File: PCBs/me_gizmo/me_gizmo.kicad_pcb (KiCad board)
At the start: 2 copper layers, 28.5 x 63.8 mm, 36 parts, among them J2 Conn_01x24_Pin, J3 Conn_01x09_Pin, J4 Conn_01x07_Pin, U1 ADG714, U2 ADG714, U3 ADG714, U4 ADG714, U5 XS3A4053, U6 XS3A4053

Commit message: First draft on the schematic for the final device
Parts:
- added C1: 1µF, Capacitor_SMD:C_0402_1005Metric, F.Cu at (63.0, 69.3)
- added C10: 0.1µF, Capacitor_SMD:C_0402_1005Metric, F.Cu at (65.9, 73.3)
- added C11: 4.7µF, Eclectronics:C_0402_1005Metric, F.Cu at (65.9, 75.2)
- added C12: 4.7µF, Capacitor_SMD:C_0402_1005Metric, F.Cu at (65.9, 77.2)
- added C13: 4.7µF, Eclectronics:C_0402_1005Metric, F.Cu at (68.7, 69.3)
- added C14: 0.1µF, Capacitor_SMD:C_0402_1005Metric, F.Cu at (68.7, 71.3)
- added C15: 4.7µF, Capacitor_SMD:C_0402_1005Metric, F.Cu at (68.7, 73.3)
- added C16: 0.1µF, Capacitor_SMD:C_0402_1005Metric, F.Cu at (68.7, 75.2)
- added C17: 1µF, Capacitor_SMD:C_0603_1608Metric, F.Cu at (54.8, 84.6)
- added C18: 1µF, Capacitor_SMD:C_0603_1608Metric, F.Cu at (54.8, 87.1)
- added C19: 0.1µF, Capacitor_SMD:C_0603_1608Metric, F.Cu at (54.8, 89.6)
- added C2: 10µF, Capacitor_SMD:C_0603_1608Metric, F.Cu at (54.8, 79.5)
- added C22: 0.1µF, Capacitor_SMD:C_0603_1608Metric, F.Cu at (43.6, 99.5)
- added C23: 1µF, Capacitor_SMD:C_0603_1608Metric, F.Cu at (43.6, 102.0)
- added C24: 1µF, Capacitor_SMD:C_0603_1608Metric, F.Cu at (43.6, 104.5)
- added C25: 1µF, Capacitor_SMD:C_0603_1608Metric, F.Cu at (43.6, 107.0)
- added C26: 0.1µF, Capacitor_SMD:C_0603_1608Metric, F.Cu at (43.6, 109.5)
- added C27: 0.1µF, Capacitor_SMD:C_0603_1608Metric, F.Cu at (43.6, 112.0)
- added C28: 0.1µF, Capacitor_SMD:C_0603_1608Metric, F.Cu at (47.6, 99.5)
- added C29: 0.1µF, Capacitor_SMD:C_0603_1608Metric, F.Cu at (47.6, 102.0)
- added C3: 10µF, Capacitor_SMD:C_0603_1608Metric, F.Cu at (54.8, 82.1)
- added C30: 0.1µF, Capacitor_SMD:C_0603_1608Metric, F.Cu at (47.6, 104.5)
- added C31: 0.1µF, Capacitor_SMD:C_0603_1608Metric, F.Cu at (47.6, 107.0)
- added C32: 0.1µF, Capacitor_SMD:C_0603_1608Metric, F.Cu at (47.6, 109.5)
- added C33: 0.1µF, Capacitor_SMD:C_0603_1608Metric, F.Cu at (47.6, 112.0)
- added C34: 0.1µF, Capacitor_SMD:C_0603_1608Metric, F.Cu at (51.6, 99.5)
- added C35: 0.1µF, Capacitor_SMD:C_0603_1608Metric, F.Cu at (51.6, 102.0)
- added C36: 0.1µF, Capacitor_SMD:C_0603_1608Metric, F.Cu at (51.6, 104.5)
- added C37: 0.1µF, Capacitor_SMD:C_0603_1608Metric, F.Cu at (51.6, 107.0)
- added C4: 0.1µF, Capacitor_SMD:C_0402_1005Metric, F.Cu at (63.0, 71.3)
- added C41: 0.1u, Capacitor_SMD:C_0603_1608Metric, F.Cu at (95.3, 99.5)
- added C42: 0.1u, Capacitor_SMD:C_0603_1608Metric, F.Cu at (95.3, 102.0)
- added C43: 0.1u, Capacitor_SMD:C_0603_1608Metric, F.Cu at (95.3, 104.5)
- added C44: 0.1u, Capacitor_SMD:C_0603_1608Metric, F.Cu at (95.3, 107.0)
- added C5: 0.1µF, Capacitor_SMD:C_0402_1005Metric, F.Cu at (63.0, 73.3)
- added C6: 0.1µF, Capacitor_SMD:C_0402_1005Metric, F.Cu at (63.0, 75.2)
- added C7: 0.1µF, Capacitor_SMD:C_0402_1005Metric, F.Cu at (63.0, 77.2)
- added C8: 0.1µF, Capacitor_SMD:C_0402_1005Metric, F.Cu at (65.9, 69.3)
- added C9: 0.1µF, Capacitor_SMD:C_0402_1005Metric, F.Cu at (65.9, 71.3)
- added D1: LED, LED_SMD:LED_0805_2012Metric, F.Cu at (69.5, 79.8)
- added D2: IN-S85TATRGB, Eclectronics:IN-S85TATRGB, F.Cu at (69.9, 85.7)
- added D3: PWR, LED_SMD:LED_0805_2012Metric, F.Cu at (69.5, 82.8)
- added J1: PushButton_Terminal_01x06, Eclectronics:CONN5_233-505_WAG, F.Cu at (79.7, 81.0)
- added J5: DEBUG, Connector_PinHeader_2.54mm:PinHeader_1x03_P2.54mm_Vertical, F.Cu at (65.0, 80.6)
- added J6: USB4105-GF-A, Eclectronics:USB4105-GF-A, F.Cu at (47.2, 74.4)
- added L1: 3.3µH, Eclectronics:AOTA-B201610S3R3-101-T, F.Cu at (44.3, 93.9)
- added Q3: MBT3904DW1, Package_TO_SOT_SMD:SOT-363_SC-70-6, F.Cu at (48.6, 90.0)
- added R10: 348, Resistor_SMD:R_0603_1608Metric, F.Cu at (43.6, 124.6)
- added R11: 118, Resistor_SMD:R_0603_1608Metric, F.Cu at (43.6, 127.1)
- added R12: 118, Resistor_SMD:R_0603_1608Metric, F.Cu at (43.6, 129.6)
- added R13: 348, Resistor_SMD:R_0603_1608Metric, F.Cu at (43.6, 132.1)
- added R14: 348, Resistor_SMD:R_0603_1608Metric, F.Cu at (43.6, 134.6)
- added R15: 118, Resistor_SMD:R_0603_1608Metric, F.Cu at (43.6, 137.2)
- added R16: 348, Resistor_SMD:R_0603_1608Metric, F.Cu at (70.4, 99.5)
- added R17: 118, Resistor_SMD:R_0603_1608Metric, F.Cu at (70.4, 102.0)
- added R18: 118, Resistor_SMD:R_0603_1608Metric, F.Cu at (70.4, 104.5)
- added R4: 348, Resistor_SMD:R_0603_1608Metric, F.Cu at (94.9, 78.9)
- added R43: 100Ω, Resistor_SMD:R_0603_1608Metric, F.Cu at (55.6, 112.0)
- added R44: 5.1K, Resistor_SMD:R_0402_1005Metric, F.Cu at (57.2, 75.3)
- added R45: 1K, Resistor_SMD:R_0402_1005Metric, F.Cu at (57.2, 77.3)
- added R46: 1K, Resistor_SMD:R_0402_1005Metric, F.Cu at (60.1, 69.3)
- added R47: 1K, Resistor_SMD:R_0402_1005Metric, F.Cu at (60.1, 71.3)
- added R48: 10k, Resistor_SMD:R_0402_1005Metric, F.Cu at (60.1, 73.3)
- added R5: 118, Resistor_SMD:R_0603_1608Metric, F.Cu at (94.9, 81.5)
- added R6: 118, Resistor_SMD:R_0603_1608Metric, F.Cu at (94.9, 84.0)
- added R7: 348, Resistor_SMD:R_0603_1608Metric, F.Cu at (94.9, 86.5)
- added R8: 348, Resistor_SMD:R_0603_1608Metric, F.Cu at (94.9, 89.0)
- added R9: 118, Resistor_SMD:R_0603_1608Metric, F.Cu at (94.9, 91.5)
- added S1: RST, Button_Switch_SMD:SW_SPST_B3U-1000P, F.Cu at (59.8, 80.5)
- added S2: BOOT, Button_Switch_SMD:SW_SPST_B3U-1000P, F.Cu at (59.8, 84.8)
- added U10: RP2350A, Eclectronics:RP2350A_QFN-60_EP_7.75x7.75_Pitch0.4mm, F.Cu at (116.6, 94.4)
- added U11: MCP4922, Package_SO:TSSOP-14_4.4x5mm_P0.65mm, F.Cu at (62.0, 101.5)
- added U12: MCP4922, Package_SO:TSSOP-14_4.4x5mm_P0.65mm, F.Cu at (62.0, 108.1)
- added U13: MCP1702T-3302E_CB, Package_TO_SOT_SMD:SOT-23, F.Cu at (44.0, 90.4)
- added U7: TLV9152VSSOP, Package_SO:VSSOP-8_3x3mm_P0.65mm, F.Cu at (66.4, 90.3)
- added U9: MCP3564R, Package_SO:TSSOP-20_4.4x6.5mm_P0.65mm, F.Cu at (46.3, 117.3)
- added X1: IQXO-791, Eclectronics:IQXO-791, F.Cu at (49.0, 93.5)
- added X4: SG-8018CG_19.6608M-TJHSA3, Crystal:Crystal_SMD_2520-4Pin_2.5x2.0mm, F.Cu at (53.0, 115.3)
- J2: value Conn_01x24_Pin -> PushButton_Terminal_01x06; footprint Connector_PinHeader_2.54mm:PinHeader_1x24_P2.54mm_Vertical -> Eclectronics:CONN5_233-505_WAG
- J3: value Conn_01x09_Pin -> PushButton_Terminal_01x06; footprint Connector_PinHeader_2.54mm:PinHeader_1x09_P2.54mm_Vertical -> Eclectronics:CONN5_233-505_WAG
- J4: value Conn_01x07_Pin -> PushButton_Terminal_01x06; footprint Connector_PinHeader_2.54mm:PinHeader_1x07_P2.54mm_Vertical -> Eclectronics:CONN5_233-505_WAG
- R1, R2, R3: value R -> 10k; footprint Resistor_SMD:R_0603_1608Metric -> Resistor_SMD:R_0402_1005Metric_Pad0.72x0.64mm_HandSolder
- R19, R20, R22: value 120 -> 348
- R21: value 120 -> 118
- R23, R24, R27: value 350 -> 118
- R25, R26: value 350 -> 348
- R28, R29, R30, R31: value 350 -> 5.1K; footprint Resistor_SMD:R_0603_1608Metric -> Resistor_SMD:R_0402_1005Metric
- R32, R33: value 350 -> 27Ω; footprint Resistor_SMD:R_0603_1608Metric -> Resistor_SMD:R_0402_1005Metric
- R34: value 350 -> 33Ω; footprint Resistor_SMD:R_0603_1608Metric -> Resistor_SMD:R_0402_1005Metric
- R35: value 120 -> 1K; footprint Resistor_SMD:R_0603_1608Metric -> Resistor_SMD:R_0402_1005Metric
- R36, R37, R38, R39, R40, R41, R42: value 120 -> 100Ω
- U5: value XS3A4053 -> REF35250QDBVR; footprint Multiplexer:TSSOP-16 -> Package_TO_SOT_SMD:SOT-23-6
- U6: value XS3A4053 -> TMP126-Q1; footprint Multiplexer:TSSOP-16 -> Package_TO_SOT_SMD:SOT-23-6
- moved J2 86.6 mm to (51.3, 126.7)
- moved R28 84.4 mm to (54.3, 69.3), turned to 0 degrees
- moved R35 82.9 mm to (57.2, 73.3), turned to 0 degrees
- moved U2 80.7 mm to (87.9, 73.0), turned to 0 degrees
- moved R29 79.9 mm to (54.3, 71.3)
- moved U5 78.2 mm to (59.4, 89.4)
- moved R42 78.1 mm to (55.6, 109.5), turned to 0 degrees
- moved R40 77.6 mm to (55.6, 104.5), turned to 0 degrees
- moved R30 77.2 mm to (54.3, 73.3), turned to 0 degrees
- moved R37 76.3 mm to (51.6, 112.0)
- moved R32 76.2 mm to (54.3, 77.3), turned to 0 degrees
- moved R36 75.9 mm to (51.6, 109.5), turned to 0 degrees
- moved R41 75.4 mm to (55.6, 107.0), turned to 0 degrees
- moved R31 74.8 mm to (54.3, 75.3), turned to 0 degrees
- moved U1 73.9 mm to (78.7, 73.0), turned to 0 degrees
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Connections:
- J2 pad 1: /Wheatstone Bridge 1/HB_OUT1+ -> VREF_BUF
- J2 pad 10: /Wheatstone Bridge 1/2ADC_IN2+ -> (no net)
- J2 pad 2: /Wheatstone Bridge 1/2ADC_IN1- -> /ADC/DAC/CH2/HB2+
- J2 pad 3: /Wheatstone Bridge 1/HB_OUT1- -> /ADC/DAC/CH2/ADC2+
- J2 pad 4: /Wheatstone Bridge 1/2ADC_IN1+ -> /ADC/DAC/CH2/HB2-
- J2 pad 5: /Wheatstone Bridge 1/2.5V -> /ADC/DAC/CH2/ADC2-
- J2 pad 7: /Wheatstone Bridge 1/HB_OUT2+ -> (no net)
- J2 pad 8: /Wheatstone Bridge 1/2ADC_IN2- -> (no net)
- J2 pad 9: /Wheatstone Bridge 1/HB_OUT2- -> (no net)
- J3 pad 1: /Wheatstone Bridge 1/2ADC_IN4- -> VREF_BUF
- J3 pad 2: /Wheatstone Bridge 1/2ADC_IN4+ -> /ADC/DAC/CH3/HB3+
- J3 pad 3: /Wheatstone Bridge 1/2ADC_IN3- -> /ADC/DAC/CH3/ADC3+
- J3 pad 4: /Wheatstone Bridge 1/2ADC_IN3+ -> /ADC/DAC/CH3/HB3-
- J3 pad 5: /Wheatstone Bridge 1/2ADC_IN2- -> /ADC/DAC/CH3/ADC3-
- J3 pad 6: /Wheatstone Bridge 1/2ADC_IN2+ -> GND
- J3 pad 7: /Wheatstone Bridge 1/2ADC_IN1- -> (no net)
- J3 pad 8: /Wheatstone Bridge 1/2ADC_IN1+ -> (no net)
- J3 pad 9: /Wheatstone Bridge 1/2.5V -> (no net)
- J4 pad 1: /Wheatstone Bridge 1/CIPO -> VREF_BUF
- J4 pad 2: /Wheatstone Bridge 1/VDD -> /ADC/DAC/CH4/HB4+
- J4 pad 3: /Wheatstone Bridge 1/SCLK -> /ADC/DAC/CH4/ADC4+
- J4 pad 4: /Wheatstone Bridge 1/RESET -> /ADC/DAC/CH4/HB4-
- J4 pad 5: /Wheatstone Bridge 1/CS -> /ADC/DAC/CH4/ADC4-
- J4 pad 6: /Wheatstone Bridge 1/Rselect1 -> GND
- J4 pad 7: /Wheatstone Bridge 1/Rselect2 -> (no net)
- R1 pad 1: Net-(U2-DOUT) -> +5V
- R1 pad 2: /Wheatstone Bridge 1/VDD -> Net-(U1I-DOUT)
- R19 pad 1: /Wheatstone Bridge 1/RI1 -> GND
- R19 pad 2: /Wheatstone Bridge 1/HB_OUT3- -> Net-(U4F-D)
- R2 pad 1: /Wheatstone Bridge 1/VDD -> +5V
- R2 pad 2: Net-(U3-DOUT) -> Net-(U2I-DOUT)
- R20 pad 1: /Wheatstone Bridge 1/RJ1 -> GND
- R20 pad 2: GND -> Net-(U4E-D)
- R21 pad 1: /Wheatstone Bridge 1/RK1 -> Net-(U4D-D)
- R22 pad 1: /Wheatstone Bridge 1/RL1 -> Net-(U1C-S)
- R22 pad 2: /Wheatstone Bridge 1/HB_OUT4- -> /ADC/DAC/CH4/HB4-
- R23 pad 1: /Wheatstone Bridge 1/RI2 -> Net-(U1D-S)
- R23 pad 2: /Wheatstone Bridge 1/HB_OUT3- -> /ADC/DAC/CH4/HB4-
- R24 pad 1: /Wheatstone Bridge 1/RJ2 -> Net-(U4A-D)
- R25 pad 1: /Wheatstone Bridge 1/RK2 -> GND
- R25 pad 2: GND -> Net-(U4H-D)
- R26 pad 1: /Wheatstone Bridge 1/RL2 -> GND
- R26 pad 2: /Wheatstone Bridge 1/HB_OUT4- -> Net-(U4G-D)
- R27 pad 1: /Wheatstone Bridge 1/RH2 -> Net-(U4B-D)
- R28 pad 1: /Wheatstone Bridge 1/RG2 -> +3V3
- R28 pad 2: GND -> /RUN
- R29 pad 1: /Wheatstone Bridge 1/RF2 -> +3V3
- R29 pad 2: /Wheatstone Bridge 1/HB_OUT2- -> /BOOT
- R3 pad 1: Net-(U1-DOUT) -> +5V
- R3 pad 2: /Wheatstone Bridge 1/VDD -> Net-(U3I-DOUT)
- R30 pad 1: /Wheatstone Bridge 1/RE2 -> Net-(J6-CC2)
- R31 pad 1: /Wheatstone Bridge 1/RD2 -> Net-(J6-CC1)
- R32 pad 1: /Wheatstone Bridge 1/RC2 -> Net-(J6-D--PadA7)
- R32 pad 2: /Wheatstone Bridge 1/HB_OUT1- -> Net-(U10-USB_D-)
- R33 pad 1: /Wheatstone Bridge 1/RB2 -> Net-(J6-D+-PadA6)
- R33 pad 2: GND -> Net-(U10-USB_D+)
- R34 pad 1: /Wheatstone Bridge 1/RA2 -> Net-(U10-VREG_AVDD)
- R34 pad 2: GND -> +3V3
- R35 pad 1: /Wheatstone Bridge 1/RH1 -> /GPIO22
- R35 pad 2: GND -> Net-(D2-Pad1)
- R36 pad 1: /Wheatstone Bridge 1/RG1 -> Net-(U9-CH7)
- R36 pad 2: GND -> /ADC/DAC/CH4/ADC4-
- R37 pad 1: /Wheatstone Bridge 1/RF1 -> Net-(U9-CH6)
- R37 pad 2: /Wheatstone Bridge 1/HB_OUT2- -> /ADC/DAC/CH4/ADC4+
- R38 pad 1: /Wheatstone Bridge 1/RE1 -> Net-(U9-CH5)
- R38 pad 2: GND -> /ADC/DAC/CH3/ADC3-
- R39 pad 1: /Wheatstone Bridge 1/RD1 -> Net-(U9-CH4)
- R39 pad 2: GND -> /ADC/DAC/CH3/ADC3+
- R40 pad 1: /Wheatstone Bridge 1/RC1 -> Net-(U9-CH3)
- R40 pad 2: /Wheatstone Bridge 1/HB_OUT1- -> /ADC/DAC/CH2/ADC2-
- R41 pad 1: /Wheatstone Bridge 1/RB1 -> Net-(U9-CH2)
- R41 pad 2: GND -> /ADC/DAC/CH2/ADC2+
- R42 pad 1: /Wheatstone Bridge 1/RA1 -> Net-(U9-CH1)
- R42 pad 2: GND -> /ADC/DAC/CH1/ADC1-
- U1 pad 1: /Wheatstone Bridge 1/SCLK -> SCLK
- U1 pad 10: /Wheatstone Bridge 1/branch5 -> VREF_BUF
- U1 pad 11: /Wheatstone Bridge 1/2.5V -> Net-(U1D-S)
- U1 pad 12: /Wheatstone Bridge 1/branch4 -> VREF_BUF
- U1 pad 13: /Wheatstone Bridge 1/branch3 -> Net-(U1E-D)
- U1 pad 14: /Wheatstone Bridge 1/HB_OUT1- -> VREF_BUF
- U1 pad 15: /Wheatstone Bridge 1/branch6 -> Net-(U1F-D)
- U1 pad 16: /Wheatstone Bridge 1/HB_OUT2- -> VREF_BUF
- U1 pad 17: /Wheatstone Bridge 1/branch7 -> Net-(U1G-D)
- U1 pad 18: /Wheatstone Bridge 1/HB_OUT3+ -> VREF_BUF
- U1 pad 19: /Wheatstone Bridge 1/branch8 -> Net-(U1H-D)
- U1 pad 2: /Wheatstone Bridge 1/VDD -> +5V
- U1 pad 20: /Wheatstone Bridge 1/HB_OUT3- -> VREF_BUF
- U1 pad 22: Net-(U1-DOUT) -> Net-(U1I-DOUT)
- U1 pad 23: /Wheatstone Bridge 1/RESET -> /RESET
- U1 pad 24: /Wheatstone Bridge 1/CS -> /SYNC
- U1 pad 3: /Wheatstone Bridge 1/CIPO -> COPI
- U1 pad 5: /Wheatstone Bridge 1/HB_OUT1+ -> Net-(U1A-S)
- U1 pad 6: /Wheatstone Bridge 1/branch2 -> VREF_BUF
- U1 pad 7: /Wheatstone Bridge 1/2.5V -> Net-(U1B-S)
- U1 pad 8: /Wheatstone Bridge 1/branch1 -> VREF_BUF
- U1 pad 9: /Wheatstone Bridge 1/HB_OUT2+ -> Net-(U1C-S)
- U2 pad 1: /Wheatstone Bridge 1/SCLK -> SCLK
- U2 pad 10: /Wheatstone Bridge 1/branch10 -> Net-(U2C-D)
- U2 pad 11: /Wheatstone Bridge 1/2.5V -> Net-(U2D-S)
- U2 pad 12: /Wheatstone Bridge 1/branch9 -> /ADC/DAC/CH1/HB1+
- U2 pad 13: /Wheatstone Bridge 1/RI1 -> /ADC/DAC/CH1/HB1+
- U2 pad 14: /Wheatstone Bridge 1/branch9 -> Net-(U2E-S)
- U2 pad 15: /Wheatstone Bridge 1/RJ1 -> /ADC/DAC/CH1/HB1-
- U2 pad 16: /Wheatstone Bridge 1/branch10 -> Net-(U2F-S)
- U2 pad 17: /Wheatstone Bridge 1/RK1 -> Net-(U2G-D)
- U2 pad 18: /Wheatstone Bridge 1/branch11 -> /ADC/DAC/CH2/HB2+
- U2 pad 19: /Wheatstone Bridge 1/RL1 -> Net-(U2H-D)
- U2 pad 2: /Wheatstone Bridge 1/VDD -> +5V
- U2 pad 20: /Wheatstone Bridge 1/branch12 -> /ADC/DAC/CH2/HB2-
- U2 pad 22: Net-(U2-DOUT) -> Net-(U2I-DOUT)
- U2 pad 23: /Wheatstone Bridge 1/RESET -> /RESET
- U2 pad 24: /Wheatstone Bridge 1/CS -> /SYNC
- U2 pad 3: Net-(U1-DOUT) -> Net-(U1I-DOUT)
- U2 pad 5: /Wheatstone Bridge 1/2.5V -> /ADC/DAC/CH2/HB2-
- U2 pad 6: /Wheatstone Bridge 1/branch12 -> Net-(U2A-D)
- U2 pad 7: /Wheatstone Bridge 1/HB_OUT4- -> /ADC/DAC/CH2/HB2+
- U2 pad 8: /Wheatstone Bridge 1/branch11 -> Net-(U2B-D)
- U2 pad 9: /Wheatstone Bridge 1/HB_OUT4+ -> /ADC/DAC/CH1/HB1-
- U3 pad 1: /Wheatstone Bridge 1/SCLK -> SCLK
- U3 pad 10: /Wheatstone Bridge 1/2ADC_IN4+ -> /ADC/DAC/CH2/ADC2+
- U3 pad 11: /Wheatstone Bridge 1/HB_OUT4- -> /ADC/DAC/CH2/HB2-
- U3 pad 12: /Wheatstone Bridge 1/2ADC_IN4- -> /ADC/DAC/CH2/ADC2-
- U3 pad 13: /Wheatstone Bridge 1/2ADC_IN2- -> /ADC/DAC/CH3/ADC3+
- U3 pad 14: /Wheatstone Bridge 1/HB_OUT2- -> /ADC/DAC/CH3/HB3+
- U3 pad 15: /Wheatstone Bridge 1/2ADC_IN2+ -> /ADC/DAC/CH3/ADC3-
- U3 pad 16: /Wheatstone Bridge 1/HB_OUT2+ -> /ADC/DAC/CH3/HB3-
- U3 pad 17: /Wheatstone Bridge 1/2ADC_IN1- -> /ADC/DAC/CH4/ADC4+
- U3 pad 18: /Wheatstone Bridge 1/HB_OUT1- -> /ADC/DAC/CH4/HB4+
- U3 pad 19: /Wheatstone Bridge 1/2ADC_IN1+ -> /ADC/DAC/CH4/ADC4-
- U3 pad 2: /Wheatstone Bridge 1/VDD -> +5V
- U3 pad 20: /Wheatstone Bridge 1/HB_OUT1+ -> /ADC/DAC/CH4/HB4-
- U3 pad 22: Net-(U3-DOUT) -> Net-(U3I-DOUT)
- U3 pad 23: /Wheatstone Bridge 1/RESET -> /RESET
- U3 pad 24: /Wheatstone Bridge 1/CS -> /SYNC
- U3 pad 3: Net-(U2-DOUT) -> Net-(U2I-DOUT)
- U3 pad 5: /Wheatstone Bridge 1/HB_OUT3+ -> /ADC/DAC/CH1/HB1+
- U3 pad 6: /Wheatstone Bridge 1/2ADC_IN3+ -> /ADC/DAC/CH1/ADC1+
- U3 pad 7: /Wheatstone Bridge 1/HB_OUT3- -> /ADC/DAC/CH1/HB1-
- U3 pad 8: /Wheatstone Bridge 1/2ADC_IN3- -> /ADC/DAC/CH1/ADC1-
- U3 pad 9: /Wheatstone Bridge 1/HB_OUT4+ -> /ADC/DAC/CH2/HB2+
- U4 pad 1: /Wheatstone Bridge 1/SCLK -> SCLK
- U4 pad 10: /Wheatstone Bridge 1/RG2 -> Net-(U4C-D)
- U4 pad 11: /Wheatstone Bridge 1/branch8 -> /ADC/DAC/CH3/HB3+
- U4 pad 12: /Wheatstone Bridge 1/RH2 -> Net-(U4D-D)
- U4 pad 13: /Wheatstone Bridge 1/RI2 -> Net-(U4E-D)
- U4 pad 14: /Wheatstone Bridge 1/branch9 -> /ADC/DAC/CH3/HB3+
- U4 pad 15: /Wheatstone Bridge 1/RJ2 -> Net-(U4F-D)
- U4 pad 16: /Wheatstone Bridge 1/branch10 -> /ADC/DAC/CH3/HB3-
- U4 pad 17: /Wheatstone Bridge 1/RK2 -> Net-(U4G-D)
- U4 pad 18: /Wheatstone Bridge 1/branch11 -> /ADC/DAC/CH4/HB4+
- U4 pad 19: /Wheatstone Bridge 1/RL2 -> Net-(U4H-D)
- U4 pad 2: /Wheatstone Bridge 1/VDD -> +5V
- U4 pad 20: /Wheatstone Bridge 1/branch12 -> /ADC/DAC/CH4/HB4-
- U4 pad 23: /Wheatstone Bridge 1/RESET -> /RESET
- U4 pad 24: /Wheatstone Bridge 1/CS -> /SYNC
- U4 pad 3: Net-(U3-DOUT) -> Net-(U3I-DOUT)
- U4 pad 5: /Wheatstone Bridge 1/branch8 -> /ADC/DAC/CH4/HB4-
- U4 pad 6: /Wheatstone Bridge 1/RH1 -> Net-(U4A-D)
- U4 pad 7: /Wheatstone Bridge 1/branch7 -> /ADC/DAC/CH4/HB4+
- U4 pad 8: /Wheatstone Bridge 1/RG1 -> Net-(U4B-D)
- U4 pad 9: /Wheatstone Bridge 1/branch7 -> /ADC/DAC/CH3/HB3-
- U5 pad 1: /Wheatstone Bridge 1/RD1 -> GND
- U5 pad 2: /Wheatstone Bridge 1/RD2 -> GND
- U5 pad 3: /Wheatstone Bridge 1/RE1 -> +3V3
- U5 pad 4: /Wheatstone Bridge 1/branch6 -> +3V3
- U5 pad 5: /Wheatstone Bridge 1/RE2 -> unconnected-(U5-NR-Pad5)
- U5 pad 6: GND -> /VREF
- U6 pad 1: /Wheatstone Bridge 1/RA1 -> /TEMP_CS
- U6 pad 2: /Wheatstone Bridge 1/RA2 -> GND
- U6 pad 3: /Wheatstone Bridge 1/RB1 -> /CIPO
- U6 pad 4: /Wheatstone Bridge 1/branch3 -> SCLK
- U6 pad 5: /Wheatstone Bridge 1/RB2 -> +3V3
- U6 pad 6: GND -> +3V3
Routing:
- net /Wheatstone Bridge 1/2.5V: track 147.9 -> 0.00 mm, vias 7 -> 0
- net /Wheatstone Bridge 1/CS: track 66.0 -> 0.00 mm, vias 4 -> 0
- net /Wheatstone Bridge 1/HB_OUT1+: track 64.5 -> 0.00 mm, vias 4 -> 0
- net /Wheatstone Bridge 1/RESET: track 60.6 -> 0.00 mm, vias 4 -> 0
- net /Wheatstone Bridge 1/HB_OUT3-: track 59.7 -> 0.00 mm, vias 3 -> 0
- net /Wheatstone Bridge 1/HB_OUT4-: track 58.4 -> 0.00 mm, vias 5 -> 0
- net /Wheatstone Bridge 1/HB_OUT4+: track 50.2 -> 0.00 mm, vias 4 -> 0
- net /Wheatstone Bridge 1/VDD: track 47.6 -> 0.00 mm, vias 4 -> 0
- net Net-(U2-DOUT): track 46.9 -> 0.00 mm, vias 2 -> 0
- net /Wheatstone Bridge 1/Rselect1: track 46.8 -> 0.00 mm, vias 2 -> 0
- net /Wheatstone Bridge 1/2ADC_IN1-: track 44.9 -> 0.00 mm
- net /Wheatstone Bridge 1/Rselect2: track 43.6 -> 0.00 mm, vias 2 -> 0
- net /Wheatstone Bridge 1/branch2: track 41.8 -> 0.00 mm
- net /Wheatstone Bridge 1/2ADC_IN2-: track 41.2 -> 0.00 mm, vias 1 -> 0
- net /Wheatstone Bridge 1/HB_OUT1-: track 40.3 -> 0.00 mm, vias 2 -> 0
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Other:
- board outline removed

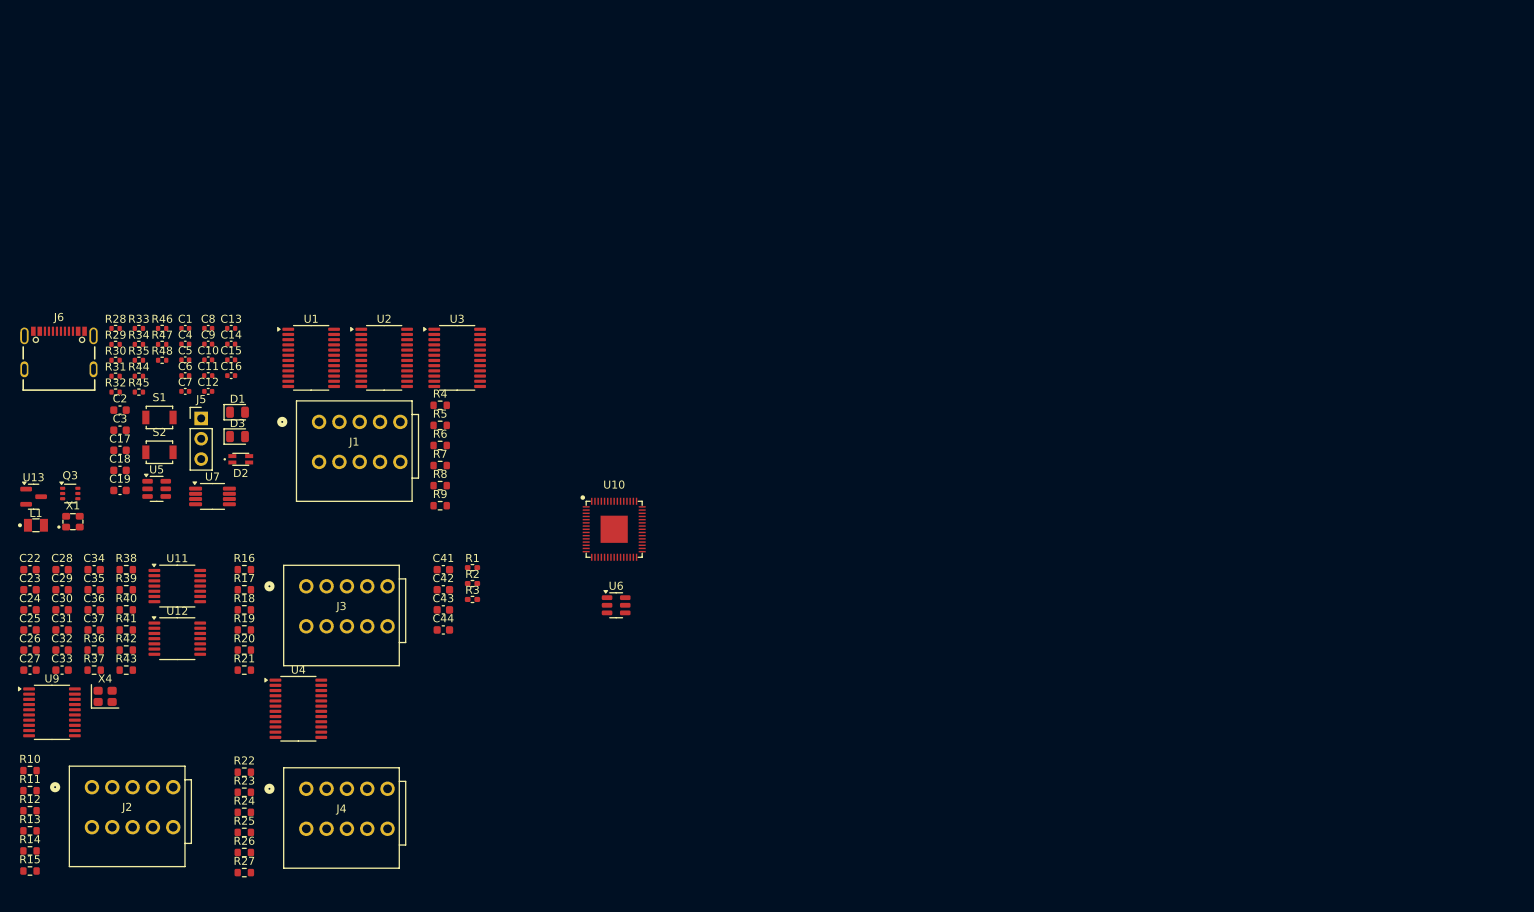
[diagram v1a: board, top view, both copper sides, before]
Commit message: Completed first draft of integrated measurement unit
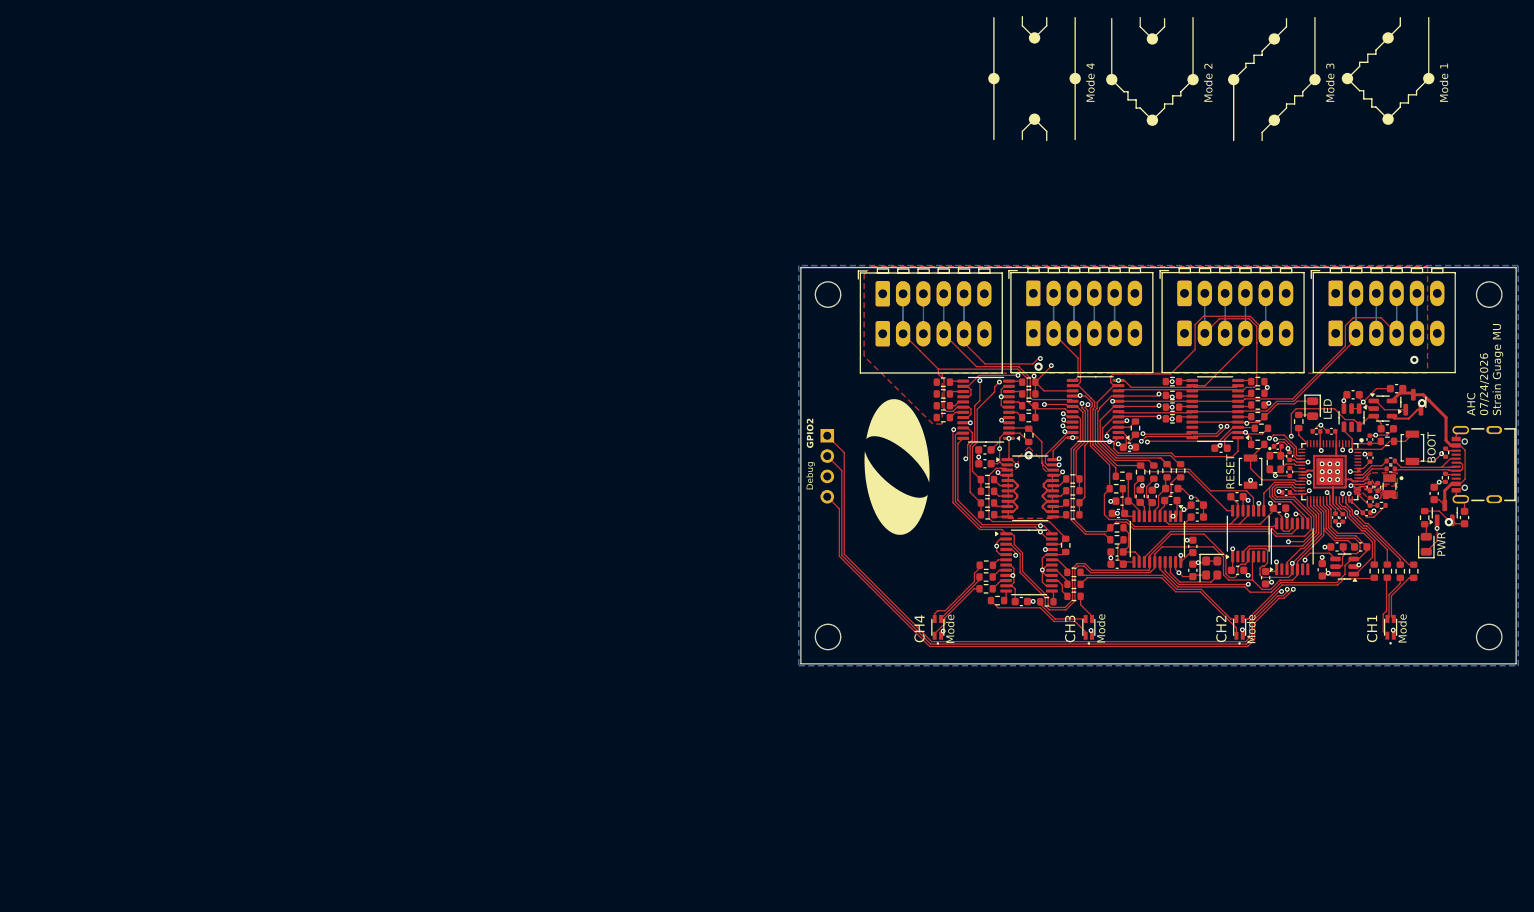
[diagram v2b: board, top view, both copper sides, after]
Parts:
- removed Q3: MBT3904DW1, Package_TO_SOT_SMD:SOT-363_SC-70-6
- added C20: 0.1µF, Capacitor_SMD:C_0603_1608Metric, F.Cu at (167.5, 103.5)
- added C45: 0.1µF, Capacitor_SMD:C_0603_1608Metric, F.Cu at (205.1, 99.5)
- added D4: IN-S85TATRGB, Eclectronics:IN-S85TATRGB, F.Cu at (213.7, 106.7)
- added D5: IN-S85TATRGB, Eclectronics:IN-S85TATRGB, F.Cu at (194.8, 106.7)
- added D6: IN-S85TATRGB, Eclectronics:IN-S85TATRGB, F.Cu at (157.1, 106.7)
- added Q1: MMBT3904L, Package_TO_SOT_SMD:SOT-23, F.Cu at (216.5, 78.6)
- added R49: 10kΩ, Capacitor_SMD:C_0603_1608Metric, F.Cu at (207.0, 96.6)
- added R50: 1kΩ, Resistor_SMD:R_0603_1608Metric, F.Cu at (213.3, 99.7)
- added R51: 5.1kΩ, Resistor_SMD:R_0603_1608Metric, F.Cu at (214.9, 99.7)
- added R52: 1kΩ, Resistor_SMD:R_0603_1608Metric, F.Cu at (216.6, 99.7)
- added R53: 1kΩ, Resistor_SMD:R_0603_1608Metric, F.Cu at (174.1, 101.3)
- added R54: 5.1kΩ, Resistor_SMD:R_0603_1608Metric, F.Cu at (174.1, 99.8)
- added R55: 1kΩ, Resistor_SMD:R_0603_1608Metric, F.Cu at (211.6, 99.7)
- added R56: 1kΩ, Resistor_SMD:R_0603_1608Metric, F.Cu at (163.1, 101.9)
- added R57: 5.1kΩ, Resistor_SMD:R_0603_1608Metric, F.Cu at (163.1, 98.9)
- added R58: 1kΩ, Resistor_SMD:R_0603_1608Metric, F.Cu at (163.1, 100.4)
- added R59: 10kΩ, Resistor_SMD:R_0603_1608Metric, F.Cu at (197.5, 81.8)
- added REF**: 4-40_hole, Eclectronics:4-40_hole, F.Cu at (226.0, 65.1)
- added REF**: 4-40_hole, Eclectronics:4-40_hole, F.Cu at (226.0, 107.9)
- added REF**: 4-40_hole, Eclectronics:4-40_hole, F.Cu at (143.3, 65.1)
- added REF**: 4-40_hole, Eclectronics:4-40_hole, F.Cu at (143.3, 107.9)
- added U8: TLV9151, Package_TO_SOT_SMD:SOT-23-5, F.Cu at (212.7, 79.3)
- added svg2mod: G***, Eclectronics:OlinLogo_0.3in, F.Cu at (152.0, 86.7)
- C41, C42, C43, C44: value 0.1u -> 0.1µF
- J1, J2, J3, J4: footprint Eclectronics:CONN5_233-505_WAG -> TerminalBlock_WAGO:TerminalBlock_WAGO_233-506_2x06_P2.54mm
- J5: value DEBUG -> Debug; footprint Connector_PinHeader_2.54mm:PinHeader_1x03_P2.54mm_Vertical -> Connector_PinHeader_2.54mm:PinHeader_1x04_P2.54mm_Vertical
- R1, R2, R3: value 10k -> 10kΩ; footprint Resistor_SMD:R_0402_1005Metric_Pad0.72x0.64mm_HandSolder -> Resistor_SMD:R_0603_1608Metric
- R10, R13, R14, R16, R19, R20, R22, R25, R26, R4, R7, R8: value 348 -> 348Ω
- R11, R12, R15, R17, R18, R21, R23, R24, R27, R5, R6, R9: value 118 -> 118Ω
- R28, R29, R44: value 5.1K -> 5.1kΩ; footprint Resistor_SMD:R_0402_1005Metric -> Resistor_SMD:R_0603_1608Metric
- R30, R31: value 5.1K -> 5.1kΩ
- R35, R45, R46, R47: value 1K -> 1kΩ; footprint Resistor_SMD:R_0402_1005Metric -> Resistor_SMD:R_0603_1608Metric
- R48: value 10k -> 10kΩ; footprint Resistor_SMD:R_0402_1005Metric -> Capacitor_SMD:C_0603_1608Metric
- S1: value RST -> RESET
- U7: value TLV9152VSSOP -> ADG714; footprint Package_SO:VSSOP-8_3x3mm_P0.65mm -> Package_SO:TSSOP-24_4.4x7.8mm_P0.65mm
- moved J6 179.8 mm to (226.6, 86.4), turned to 90 degrees
- moved U13 176.4 mm to (220.4, 92.4), turned to 90 degrees
- moved L1 169.3 mm to (213.5, 89.1), turned to -90 degrees
- moved C3 168.4 mm to (222.9, 93.0), turned to 90 degrees
- moved R31 166.7 mm to (220.5, 88.0), turned to -90 degrees
- moved R30 166.7 mm to (220.6, 84.9), turned to -90 degrees
- moved C2 164.6 mm to (219.1, 90.0), turned to -90 degrees
- moved R14 163.8 mm to (197.1, 77.4)
- moved R13 163.4 mm to (197.1, 76.0), turned to 180 degrees
- moved C19 160.1 mm to (214.4, 76.9), turned to 180 degrees
- moved R32 159.7 mm to (213.7, 86.9), turned to 180 degrees
- moved R29 159.4 mm to (213.3, 83.5)
- moved R47 159.3 mm to (217.9, 93.0), turned to -90 degrees
- moved C18 158.5 mm to (213.3, 81.9)
- moved R33 157.4 mm to (213.7, 85.9), turned to 180 degrees
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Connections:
- C18 pad 1: /VREF -> VREF
- C19 pad 1: +5V -> VBUS
- C2 pad 2: +5V -> VBUS
- C24 pad 1: /VREF -> VREF
- C34 pad 1: /VREF -> VREF
- C36 pad 1: /VREF -> VREF
- C41 pad 1: +5V -> +3V3
- C42 pad 1: +5V -> +3V3
- C43 pad 1: +5V -> +3V3
- C44 pad 1: +5V -> +3V3
- J1 pad 5: /ADC/DAC/CH1/ADC1+ -> /ADC/DAC/CH1/ADC1-
- J5 pad 1: /SWCLK -> /GPIO2
- J5 pad 2: GND -> /SWCLK
- J5 pad 3: /SWDIO -> GND
- J6 pad A4B9: +5V -> VBUS
- J6 pad B4A9: +5V -> VBUS
- R1 pad 1: +5V -> +3V3
- R1 pad 2: Net-(U1I-DOUT) -> Net-(U1I-DIN)
- R12 pad 1: Net-(U2A-D) -> Net-(U2E-D)
- R13 pad 2: Net-(U2H-D) -> Net-(U2D-D)
- R14 pad 1: Net-(U2G-D) -> Net-(U2C-S)
- R15 pad 1: Net-(U2B-D) -> Net-(U2F-S)
- R16 pad 1: Net-(U1A-S) -> Net-(U4D-D)
- R17 pad 1: Net-(U1B-S) -> Net-(U4C-D)
- R18 pad 1: Net-(U4C-D) -> Net-(U4F-D)
- R18 pad 2: GND -> VREF_BUF
- R19 pad 1: GND -> VREF_BUF
- R19 pad 2: Net-(U4F-D) -> Net-(U4E-D)
- R2 pad 1: +5V -> +3V3
- R2 pad 2: Net-(U2I-DOUT) -> Net-(U1I-DOUT)
- R20 pad 1: GND -> Net-(U1A-D)
- R20 pad 2: Net-(U4E-D) -> /ADC/DAC/CH3/HB3+
- R21 pad 1: Net-(U4D-D) -> /ADC/DAC/CH3/HB3+
- R21 pad 2: GND -> Net-(U1B-D)
- R22 pad 1: Net-(U1C-S) -> Net-(U4B-D)
- R22 pad 2: /ADC/DAC/CH4/HB4- -> /ADC/DAC/CH4/HB4+
- R23 pad 1: Net-(U1D-S) -> Net-(U4A-D)
- R23 pad 2: /ADC/DAC/CH4/HB4- -> /ADC/DAC/CH4/HB4+
- R24 pad 1: Net-(U4A-D) -> Net-(U4H-D)
- R24 pad 2: GND -> VREF_BUF
- R25 pad 1: GND -> VREF_BUF
- R25 pad 2: Net-(U4H-D) -> Net-(U4G-D)
- R26 pad 1: GND -> Net-(U1C-D)
- R26 pad 2: Net-(U4G-D) -> /ADC/DAC/CH4/HB4-
- R27 pad 1: Net-(U4B-D) -> /ADC/DAC/CH4/HB4-
- R27 pad 2: GND -> Net-(U1D-D)
- R3 pad 1: +5V -> +3V3
- R3 pad 2: Net-(U3I-DOUT) -> Net-(U3I-DIN)
- R35 pad 1: /GPIO22 -> Net-(U7D-D)
- R44 pad 1: /GPIO23 -> Net-(U7E-D)
- R45 pad 1: /GPIO24 -> Net-(U7F-D)
- R46 pad 1: /GPIO25 -> /GPIO11
- R6 pad 1: Net-(U2C-D) -> Net-(U2B-S)
- R7 pad 2: Net-(U2F-S) -> Net-(U2G-S)
- R8 pad 2: Net-(U2E-S) -> Net-(U2A-S)
- R9 pad 1: Net-(U2D-S) -> Net-(U2H-S)
- U1 pad 10: VREF_BUF -> Net-(U1C-D)
- U1 pad 11: Net-(U1D-S) -> VREF_BUF
- U1 pad 12: VREF_BUF -> Net-(U1D-D)
- U1 pad 2: +5V -> +3V3
- U1 pad 3: COPI -> Net-(U1I-DIN)
- U1 pad 5: Net-(U1A-S) -> VREF_BUF
- U1 pad 6: VREF_BUF -> Net-(U1A-D)
- U1 pad 7: Net-(U1B-S) -> VREF_BUF
- U1 pad 8: VREF_BUF -> Net-(U1B-D)
- U1 pad 9: Net-(U1C-S) -> VREF_BUF
- U10 pad 15: unconnected-(U10-GPIO11-Pad15) -> /GPIO11
- U10 pad 16: /TEMP_CS -> unconnected-(U10-GPIO12-Pad16)
- U10 pad 17: +3V3 -> unconnected-(U10-GPIO13-Pad17)
- U10 pad 27: /CIPO -> /~{LDAC}
- U10 pad 29: SCLK -> /~{IRQ}/MDAT
- U10 pad 31: COPI -> /~{DAC1_CS}
- U10 pad 32: /~{IRQ}/MDAT -> /~{DAC2_CS}
- U10 pad 33: /~{DAC1_CS} -> SCLK
- U10 pad 34: /GPIO22 -> COPI
- U10 pad 35: /GPIO23 -> /TEMP_ALERT
- U10 pad 36: /GPIO24 -> /CIPO
- U10 pad 37: /GPIO25 -> /TEMP_CS
- U10 pad 4: unconnected-(U10-GPIO2-Pad4) -> /GPIO2
- U10 pad 40: /~{DAC2_CS} -> /GPIO26
- U10 pad 41: unconnected-(U10-GPIO27/ADC1-Pad41) -> /GPIO27
- U10 pad 42: /~{LDAC} -> /GPIO28
- U10 pad 43: unconnected-(U10-GPIO29/ADC3-Pad43) -> /GPIO29
- U11 pad 10: /ADC/DAC/CH2/ADC2- -> /ADC/DAC/CH1/ADC1-
- U11 pad 11: /VREF -> VREF
- U11 pad 13: /VREF -> VREF
- U11 pad 14: /ADC/DAC/CH1/ADC1- -> /ADC/DAC/CH2/ADC2-
- U12 pad 11: /VREF -> VREF
- U12 pad 13: /VREF -> VREF
- U13 pad 3: +5V -> VBUS
- U2 pad 10: Net-(U2C-D) -> /ADC/DAC/CH2/HB2+
- U2 pad 11: Net-(U2D-S) -> /ADC/DAC/CH2/HB2-
- U2 pad 12: /ADC/DAC/CH1/HB1+ -> Net-(U2D-D)
- U2 pad 13: /ADC/DAC/CH1/HB1+ -> Net-(U2E-D)
- U2 pad 14: Net-(U2E-S) -> /ADC/DAC/CH2/HB2-
- U2 pad 15: /ADC/DAC/CH1/HB1- -> /ADC/DAC/CH2/HB2+
- U2 pad 17: Net-(U2G-D) -> /ADC/DAC/CH1/HB1-
- U2 pad 18: /ADC/DAC/CH2/HB2+ -> Net-(U2G-S)
- U2 pad 19: Net-(U2H-D) -> /ADC/DAC/CH1/HB1+
- U2 pad 2: +5V -> +3V3
- U2 pad 20: /ADC/DAC/CH2/HB2- -> Net-(U2H-S)
- U2 pad 22: Net-(U2I-DOUT) -> unconnected-(U2I-DOUT-Pad22)
- U2 pad 3: Net-(U1I-DOUT) -> Net-(U2I-DIN)
- U2 pad 5: /ADC/DAC/CH2/HB2- -> Net-(U2A-S)
- U2 pad 6: Net-(U2A-D) -> /ADC/DAC/CH1/HB1+
- U2 pad 7: /ADC/DAC/CH2/HB2+ -> Net-(U2B-S)
- U2 pad 8: Net-(U2B-D) -> /ADC/DAC/CH1/HB1-
- U2 pad 9: /ADC/DAC/CH1/HB1- -> Net-(U2C-S)
- U3 pad 10: /ADC/DAC/CH2/ADC2+ -> /ADC/DAC/CH2/HB2+
- U3 pad 11: /ADC/DAC/CH2/HB2- -> /ADC/DAC/CH2/ADC2-
- U3 pad 12: /ADC/DAC/CH2/ADC2- -> /ADC/DAC/CH2/HB2-
- U3 pad 13: /ADC/DAC/CH3/ADC3+ -> /ADC/DAC/CH3/HB3+
- U3 pad 14: /ADC/DAC/CH3/HB3+ -> /ADC/DAC/CH3/ADC3+
- U3 pad 15: /ADC/DAC/CH3/ADC3- -> /ADC/DAC/CH3/HB3-
- U3 pad 16: /ADC/DAC/CH3/HB3- -> /ADC/DAC/CH3/ADC3-
- U3 pad 17: /ADC/DAC/CH4/ADC4+ -> /ADC/DAC/CH4/HB4-
- U3 pad 18: /ADC/DAC/CH4/HB4+ -> /ADC/DAC/CH4/ADC4-
- U3 pad 19: /ADC/DAC/CH4/ADC4- -> /ADC/DAC/CH4/HB4+
- U3 pad 2: +5V -> +3V3
- U3 pad 20: /ADC/DAC/CH4/HB4- -> /ADC/DAC/CH4/ADC4+
- U3 pad 22: Net-(U3I-DOUT) -> Net-(U2I-DIN)
- U3 pad 3: Net-(U2I-DOUT) -> Net-(U3I-DIN)
- U3 pad 5: /ADC/DAC/CH1/HB1+ -> /ADC/DAC/CH1/ADC1+
- U3 pad 6: /ADC/DAC/CH1/ADC1+ -> /ADC/DAC/CH1/HB1+
- U3 pad 7: /ADC/DAC/CH1/HB1- -> /ADC/DAC/CH1/ADC1-
- U3 pad 8: /ADC/DAC/CH1/ADC1- -> /ADC/DAC/CH1/HB1-
- U3 pad 9: /ADC/DAC/CH2/HB2+ -> /ADC/DAC/CH2/ADC2+
- U4 pad 11: /ADC/DAC/CH3/HB3+ -> GND
- U4 pad 14: /ADC/DAC/CH3/HB3+ -> /ADC/DAC/CH3/HB3-
- U4 pad 2: +5V -> +3V3
- U4 pad 20: /ADC/DAC/CH4/HB4- -> /ADC/DAC/CH4/HB4+
- U4 pad 22: unconnected-(U4I-DOUT-Pad22) -> Net-(U3I-DIN)
- U4 pad 3: Net-(U3I-DOUT) -> Net-(U1I-DOUT)
- U4 pad 5: /ADC/DAC/CH4/HB4- -> GND
- U4 pad 7: /ADC/DAC/CH4/HB4+ -> GND
- U4 pad 9: /ADC/DAC/CH3/HB3- -> GND
- U5 pad 6: /VREF -> VREF
- U6 pad 5: +3V3 -> /TEMP_ALERT
- U7 pad 1: Net-(Q3A-B1) -> SCLK
- U7 pad 2: Net-(Q3A-B1) -> +3V3
- U7 pad 3: /VREF -> COPI
- U7 pad 5: /VREF -> +3V3
- U7 pad 6: Net-(Q3B-B2) -> Net-(U7A-D)
- U7 pad 7: Net-(Q3B-B2) -> +3V3
- U7 pad 8: +5V -> Net-(U7B-D)
- U9 pad 4: /VREF -> VREF
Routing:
- net SCLK: track 0.00 -> 142.3 mm, vias 0 -> 6
- net +3V3: track 0.00 -> 115.1 mm, vias 0 -> 29
- net GND: track 0.00 -> 110.4 mm, vias 0 -> 58
- net /GPIO2: track 0.00 -> 101.4 mm, vias 0 -> 2
- net /SWCLK: track 0.00 -> 94.5 mm, vias 0 -> 2
- net /SWDIO: track 0.00 -> 89.8 mm, vias 0 -> 2
- net /ADC/DAC/CH1/ADC1-: track 0.00 -> 77.4 mm, vias 0 -> 1
- net /RESET: track 0.00 -> 75.0 mm, vias 0 -> 6
- net /ADC/DAC/CH4/ADC4-: track 0.00 -> 72.6 mm, vias 0 -> 2
- net COPI: track 0.00 -> 72.4 mm
- net /SYNC: track 0.00 -> 68.8 mm, vias 0 -> 6
- net /ADC/DAC/CH1/HB1-: track 0.00 -> 65.1 mm, vias 0 -> 2
- net /ADC/DAC/CH2/ADC2-: track 0.00 -> 61.1 mm
- net /ADC/DAC/CH4/ADC4+: track 0.00 -> 58.1 mm, vias 0 -> 1
- net /ADC/DAC/CH1/ADC1+: track 0.00 -> 57.7 mm, vias 0 -> 1
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- added copper zone on F.Cu, net +1V1
- added copper zone on In2.Cu, net +3V3
- added copper zone on B.Cu, net GND
- added copper zone on F.Cu, net GND
- added copper zone on In1.Cu, net GND
- added copper zone on F.Cu, net Net-(U10-VREG_LX)
- added copper zone on F.Cu, net VREF_BUF
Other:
- board outline added: 89.4 x 49.5 mm
- copper layers 2 -> 4
- board text added: "ADC+"
- board text added: "ADC-"
- board text added: "AHC 07/24/2026 Strain Guage MU"
- board text added: "CH 1,2"
- board text added: "CH 3,4"
- board text added: "CH1"
- board text added: "CH2"
- board text added: "CH3"
- board text added: "CH4"
- board text added: "GND"
- board text added: "GPIO2"
- board text added: "HB+"
- board text added: "HB-"
- board text added: "LED"
- board text added: "Mode"
- board text added: "Mode 1"
- board text added: "Mode 2"
- board text added: "Mode 3"
- board text added: "Mode 4"
- board text added: "R18"
- board text added: "R24"
- board text added: "VREF"

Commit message: Second draft of final layout
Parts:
- S1: value RESET -> RST
- moved R30 1.15 mm to (220.6, 83.7), turned to 90 degrees
- moved C42 0.97 mm to (163.9, 84.4)
- moved C8 0.89 mm to (211.6, 92.4)
- moved R31 0.57 mm to (220.1, 87.7), turned to 180 degrees
- moved C19 0.31 mm to (214.1, 76.9)
- moved C41 0.21 mm to (162.9, 86.1)
- moved C23 0.18 mm to (188.8, 96.6)
- moved C1 0.08 mm to (199.6, 84.1)
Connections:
- R16 pad 2: /ADC/DAC/CH3/HB3- -> /ADC/DAC/CH3/HB3+
- R17 pad 2: /ADC/DAC/CH3/HB3- -> /ADC/DAC/CH3/HB3+
- R20 pad 2: /ADC/DAC/CH3/HB3+ -> /ADC/DAC/CH3/HB3-
- R21 pad 1: /ADC/DAC/CH3/HB3+ -> /ADC/DAC/CH3/HB3-
- U4 pad 14: /ADC/DAC/CH3/HB3- -> /ADC/DAC/CH3/HB3+
- U4 pad 16: /ADC/DAC/CH3/HB3- -> /ADC/DAC/CH3/HB3+
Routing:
- net GND: track 110.4 -> 66.6 mm, vias 58 -> 77
- net +3V3: track 115.1 -> 81.7 mm, vias 29 -> 43
- net /ADC/DAC/CH4/ADC4+: track 58.1 -> 49.0 mm, vias 1 -> 2
- net /ADC/DAC/CH3/HB3-: track 36.5 -> 41.5 mm, vias 3 -> 2
- net VBUS: track 24.4 -> 28.8 mm
- net /ADC/DAC/CH4/ADC4-: track 72.6 -> 68.8 mm, vias 2 -> 1
- net /ADC/DAC/CH4/HB4-: track 51.6 -> 55.2 mm
- net /ADC/DAC/CH3/HB3+: track 38.0 -> 34.6 mm
- net VREF: track 55.3 -> 53.5 mm
- net COPI: track 72.4 -> 73.8 mm
- net /SYNC: track 68.8 -> 69.9 mm
- net Net-(D5-Pad1): track 23.4 -> 22.5 mm
- net VREF_BUF: track 40.5 -> 41.4 mm
- net /CIPO: track 40.8 -> 41.6 mm
- net Net-(D6-Pad2): track 9.63 -> 9.05 mm
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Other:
- board text added: "3wire+"
- board text added: "3wire-"
- board text added: "C41"
- board text removed: "ADC+"
- board text removed: "ADC-"
- board text removed: "Mode 1"
- board text removed: "Mode 2"
- board text removed: "Mode 3"
- board text removed: "Mode 4"

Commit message: Made a few final layout tweaks and added a BOM file
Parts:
- R30, R31: footprint Resistor_SMD:R_0402_1005Metric -> Resistor_SMD:R_0603_1608Metric
- R48, R49: footprint Capacitor_SMD:C_0603_1608Metric -> Resistor_SMD:R_0603_1608Metric
- moved R31 0.53 mm to (219.6, 87.8)
- moved svg2mod 0.46 mm to (151.5, 86.5)
- moved R30 0.29 mm to (220.3, 83.8)
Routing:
- net +3V3: track 81.7 -> 82.7 mm, vias 43 -> 42
- net /ADC/DAC/CH3/HB3+: track 34.6 -> 34.0 mm
